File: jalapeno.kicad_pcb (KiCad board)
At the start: 2 copper layers, 230.1 x 77.6 mm, 187 parts, among them IC1 ATMEGA32U4-AU, J1 USB_B, J2 AVR-ISP-6, J3 Conn_01x04, K1 esc, K10 o, K11 p, K12 back, K13 tab, K14 a, K15 s, K16 d, K17 f, K18 g, K19 h, K2 q, K20 j, K21 k, K22 l, K23 ;, K24 caps, K25 caps, K26 z, K27 x, K28 c, K29 v, K3 w, K30 b, K31 n, K32 m, K33 ,, K33_1 ,, K34 ., K34_1 ., K35 ctrl, K36 gui, K37 alt, K37_1 alt, K38 space, K38_1 space, K39 alt, K39_1 gui, K4 e, K40 gui, K41 ctrl, K42 KEYSW, K5 r, K6 t, K7 y, K8 u, K9 i, Q1 MMBT2222ALT3G, SW1 SW_PUSH, U1 MDBT40, U2 SPX3819M5-L-3-3, U3 MCP73831T-2ACI/OT, Y1 XTAL_GND

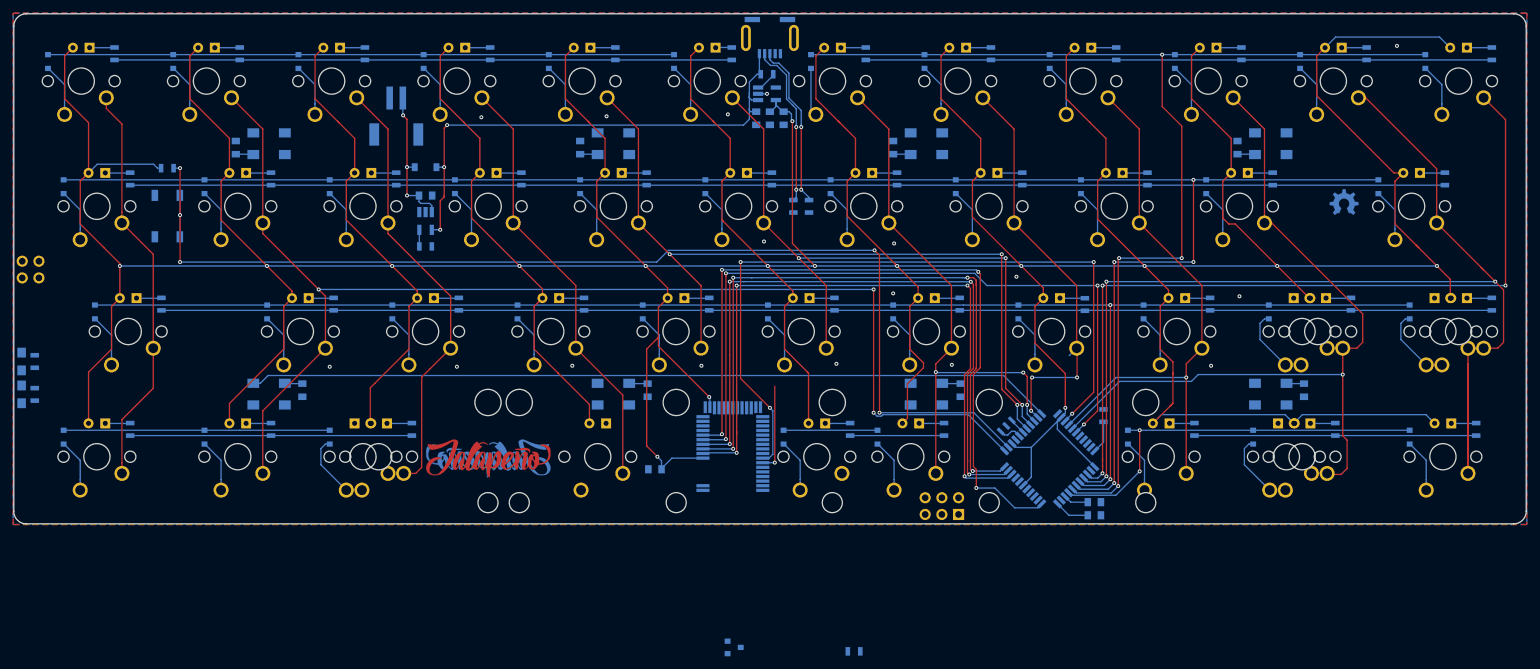
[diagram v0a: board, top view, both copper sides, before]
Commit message: routing DRC + row 4
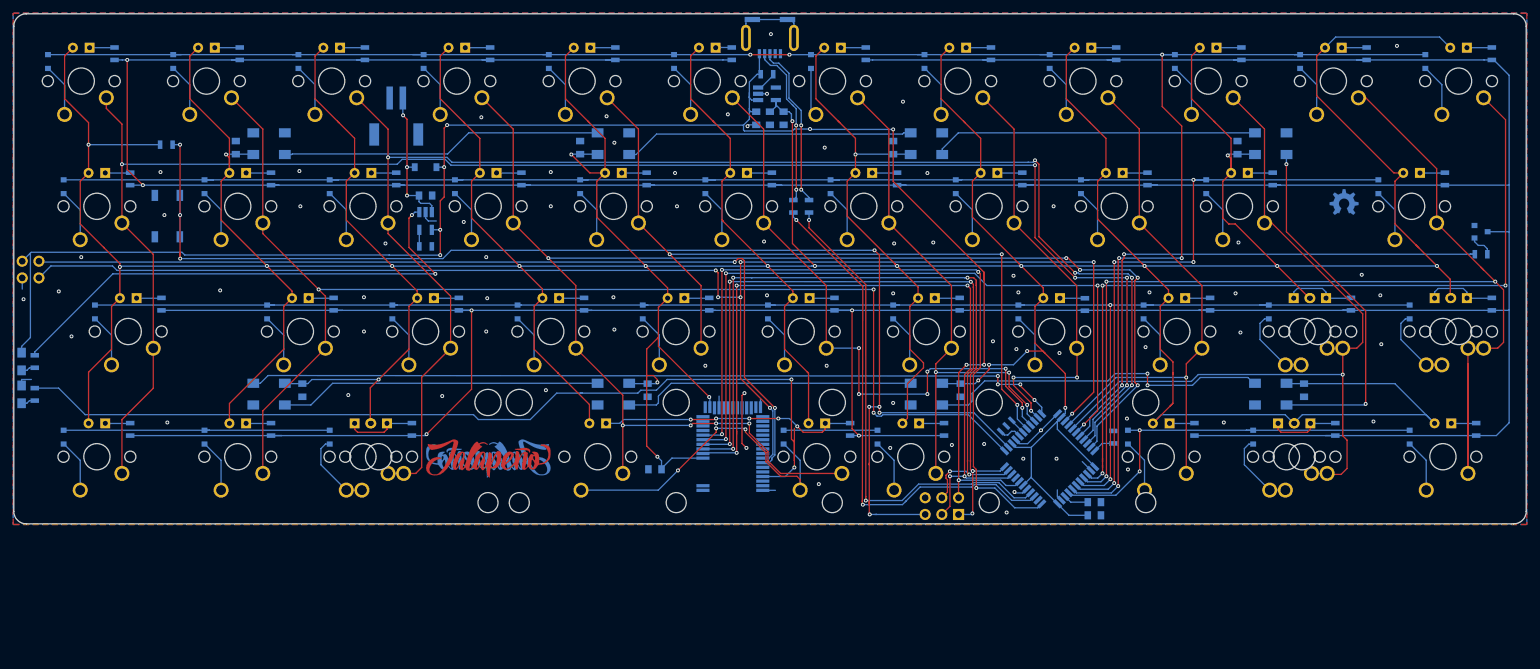
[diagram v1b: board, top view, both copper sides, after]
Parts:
- moved Q1 130.0 mm to (255.8, 56.3)
- moved R9 112.9 mm to (255.8, 59.7)
- moved R8 3.60 mm to (199.9, 87.5)
- moved R7 3.57 mm to (55.8, 43.0)
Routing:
- net COL_1: track 62.1 -> 256.6 mm, vias 0 -> 5
- net LEDGND: track 691.6 -> 876.3 mm, vias 0 -> 6
- net VBUS: track 80.0 -> 263.9 mm, vias 3 -> 9
- net COL_4: track 66.0 -> 224.8 mm, vias 0 -> 9
- net COL_3: track 67.4 -> 225.3 mm, vias 0 -> 5
- net Net-(R1-Pad2): track 0.00 -> 143.2 mm, vias 0 -> 2
- net /SWDCLK: track 12.8 -> 141.1 mm, vias 1 -> 2
- net /4_SWDIO/RST: track 112.2 -> 223.9 mm, vias 4 -> 7
- net LEDPWM: track 0.00 -> 84.4 mm, vias 0 -> 2
- net +3V3: track 1098.1 -> 1178.8 mm, vias 16 -> 26
- net Net-(R2-Pad1): track 0.00 -> 78.5 mm, vias 0 -> 2
- net Net-(IC1-Pad3): track 0.00 -> 77.8 mm, vias 0 -> 2
- net Net-(IC1-Pad4): track 0.00 -> 74.9 mm, vias 0 -> 2
- net Net-(LED4-Pad2): track 0.00 -> 55.0 mm, vias 0 -> 2
- net Net-(LED3-Pad2): track 0.00 -> 52.9 mm, vias 0 -> 2
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
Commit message: routing finalised
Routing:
- net ROW_4: track 118.1 -> 341.8 mm, vias 2 -> 11
- net GND: track 36.1 -> 55.1 mm, vias 74 -> 130
- net +3V3: track 1178.8 -> 1184.0 mm
- net Net-(R1-Pad2): track 143.2 -> 138.3 mm
